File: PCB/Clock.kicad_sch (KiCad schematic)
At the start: 24 parts, among them SW1 SW_Push, SW2 SW_SPDT, U1 LM555xM, U2 LM555xM, U3 LM555xM, U4 74LS08, U5 74LS04, U6 74LS32

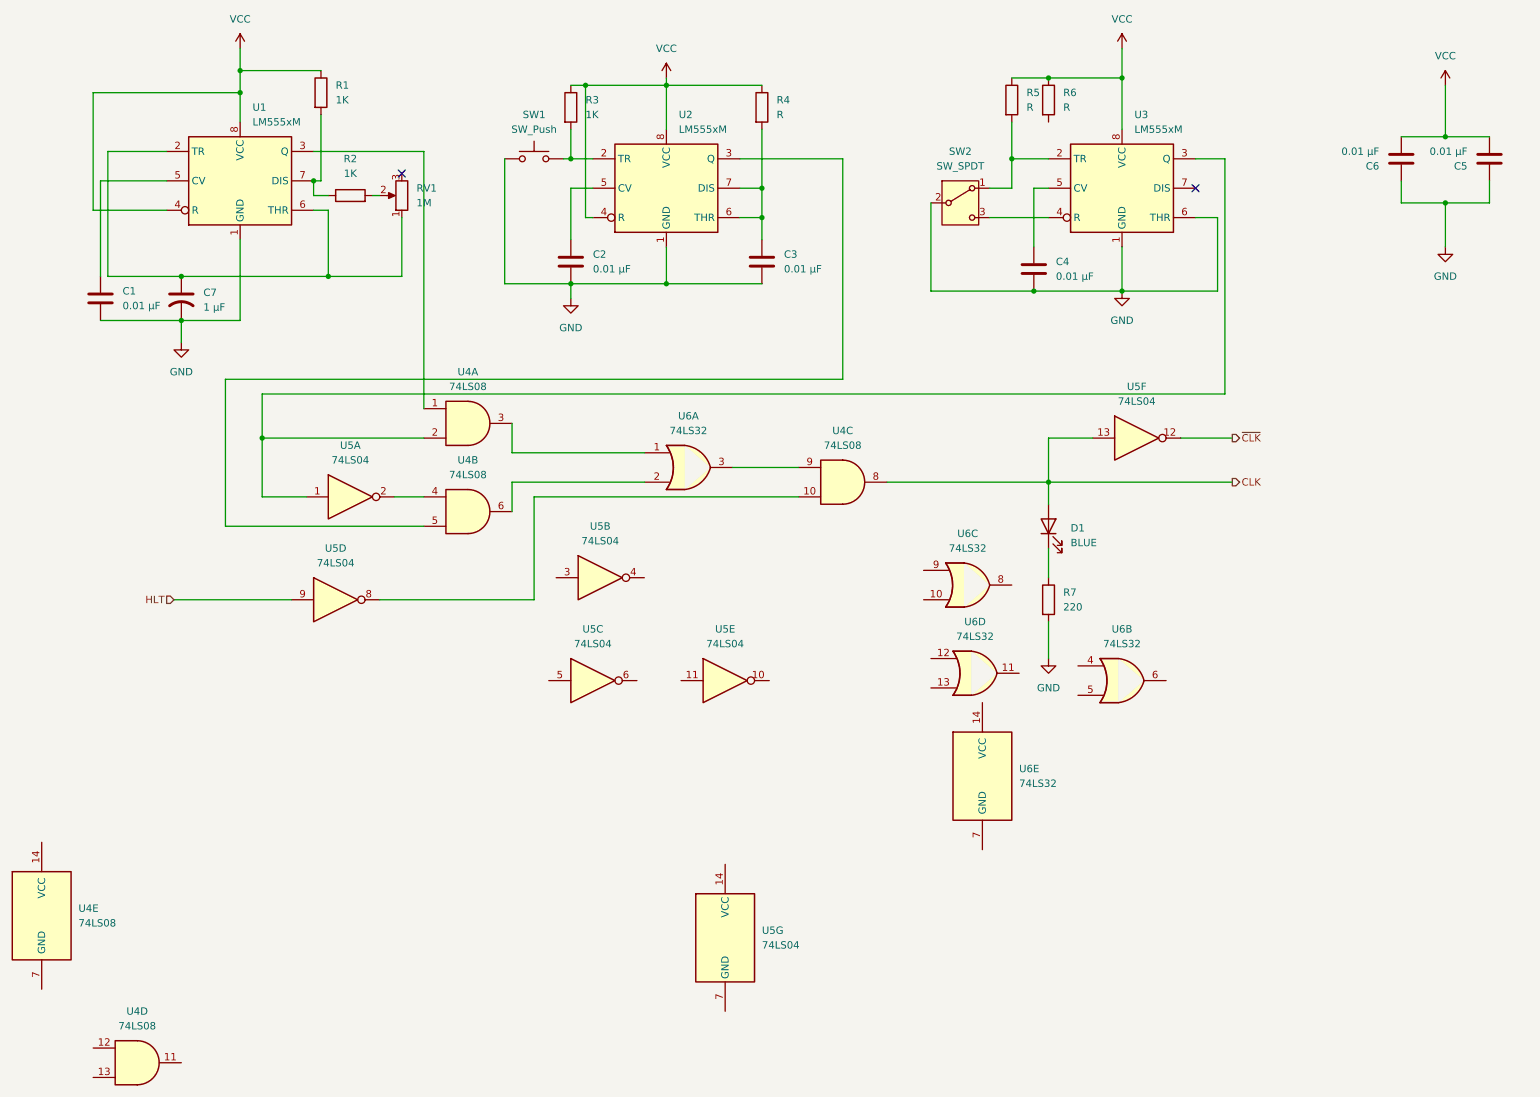
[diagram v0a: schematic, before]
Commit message: Cleaned up the schematic and got started on assigning all the footprints to the symbols
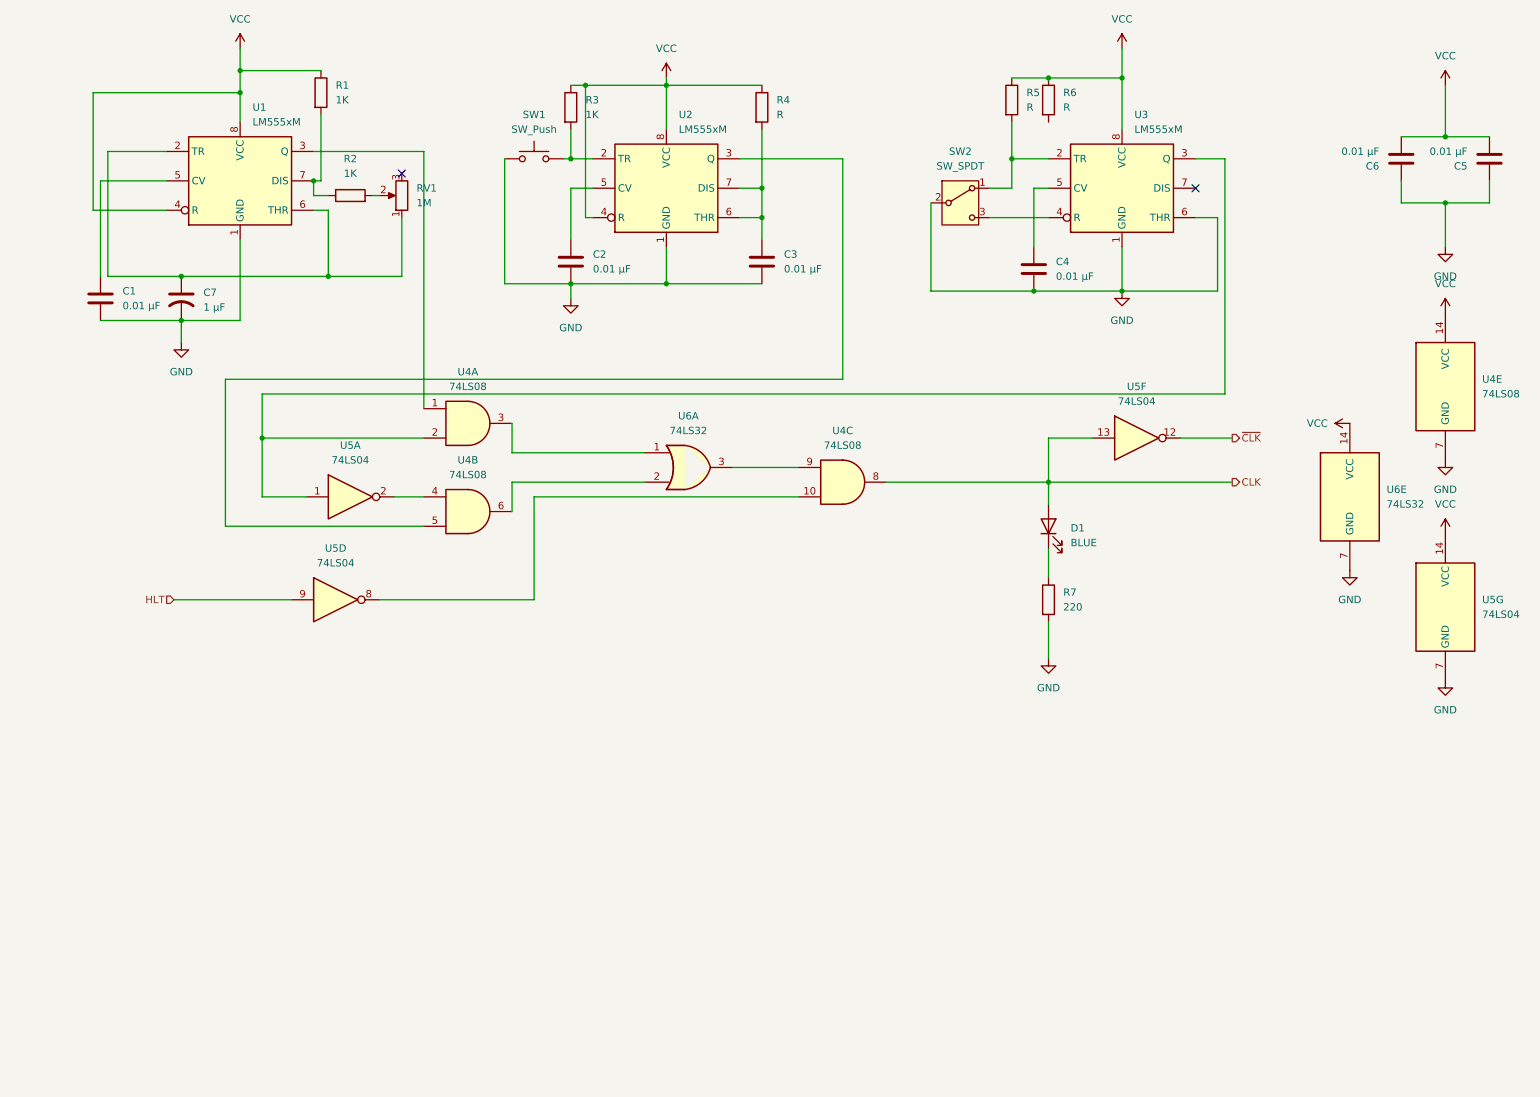
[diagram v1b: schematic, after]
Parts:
- removed unit 4 of U4
- removed unit 3 of U5
- removed unit 2 of U5
- removed unit 5 of U5
- removed unit 2 of U6
- removed unit 3 of U6
- removed unit 4 of U6
- SW1: footprint (none) -> Button_Switch_THT:SW_PUSH_6mm
- SW2: footprint (none) -> Button_Switch_SMD:SW_SPDT_CK_JS102011SAQN
- U6: footprint (none) -> footprints:N14
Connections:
- net GND: now also U4.7 (GND), U5.7 (GND), U6.7 (GND)
- net VCC: now also U4.14 (VCC), U5.14 (VCC), U6.14 (VCC)
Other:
- moved on the sheet: U4E, U5G, U6E

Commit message: added more models to work with on my pcb
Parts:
- R4: value R -> 1M
- R5, R6: value R -> 1K
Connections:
- net at R6.2: now also SW2.3 (C), U3.4 (R)
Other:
- moved on the sheet: C4, R5, R6, SW2
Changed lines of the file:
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@@
-	)
-	(junction
-		(at 193.04 59.69)
-		(diameter 0)
-		(color 0 0 0 0)
 	)
 	(junction
@@
 	)
 	(junction
-		(at 189.23 36.83)
+		(at 264.16 44.45)
 		(diameter 0)
 		(color 0 0 0 0)
 	)
 	(junction
-		(at 264.16 44.45)
+		(at 193.04 22.86)
 		(diameter 0)
 		(color 0 0 0 0)
@@
 	)
 	(junction
-		(at 195.58 22.86)
+		(at 193.04 46.99)
 		(diameter 0)
 		(color 0 0 0 0)
@@
 	)
 	(junction
+		(at 186.69 36.83)
+		(diameter 0)
+		(color 0 0 0 0)
+	)
+	(junction
 		(at 55.88 25.4)
+		(diameter 0)
+		(color 0 0 0 0)
+	)
+	(junction
+		(at 194.31 59.69)
 		(diameter 0)
 		(color 0 0 0 0)
@@
 	(wire
 		(pts
-			(xy 189.23 36.83) (xy 189.23 41.91)
+			(xy 186.69 36.83) (xy 186.69 41.91)
 		)
 		(stroke
@@
 	(wire
 		(pts
-			(xy 185.42 46.99) (xy 195.58 46.99)
+			(xy 182.88 46.99) (xy 193.04 46.99)
 		)
 		(stroke
@@
 	(wire
 		(pts
+			(xy 194.31 41.91) (xy 195.58 41.91)
+		)
+		(stroke
+			(width 0)
+			(type default)
+		)
+	)
+	(wire
+		(pts
 			(xy 45.72 57.15) (xy 71.12 57.15)
 		)
@@
 	(wire
 		(pts
+			(xy 193.04 46.99) (xy 195.58 46.99)
+		)
+		(stroke
+			(width 0)
+			(type default)
+		)
+	)
+	(wire
+		(pts
 			(xy 271.78 44.45) (xy 264.16 44.45)
 		)
@@
 	(wire
 		(pts
-			(xy 195.58 41.91) (xy 193.04 41.91)
-		)
-		(stroke
-			(width 0)
-			(type default)
-		)
-	)
-	(wire
-		(pts
 			(xy 87.63 35.56) (xy 68.58 35.56)
 		)
@@
 	(wire
 		(pts
-			(xy 189.23 30.48) (xy 189.23 36.83)
+			(xy 186.69 30.48) (xy 186.69 36.83)
 		)
 		(stroke
@@
 	(wire
 		(pts
-			(xy 193.04 59.69) (xy 208.28 59.69)
-		)
-		(stroke
-			(width 0)
-			(type default)
-		)
-	)
-	(wire
-		(pts
 			(xy 69.85 29.21) (xy 69.85 40.64)
 		)
@@
 	(wire
 		(pts
+			(xy 193.04 22.86) (xy 208.28 22.86)
+		)
+		(stroke
+			(width 0)
+			(type default)
+		)
+	)
+	(wire
+		(pts
 			(xy 129.54 58.42) (xy 113.03 58.42)
 		)
@@
 	(wire
 		(pts
-			(xy 175.26 44.45) (xy 175.26 59.69)
+			(xy 172.72 44.45) (xy 172.72 59.69)
 		)
 		(stroke
@@
 	(wire
 		(pts
-			(xy 189.23 36.83) (xy 195.58 36.83)
-		)
-		(stroke
-			(width 0)
-			(type default)
-		)
-	)
-	(wire
-		(pts
 			(xy 160.02 36.83) (xy 160.02 74.93)
 		)
@@
 	(wire
 		(pts
+			(xy 193.04 30.48) (xy 193.04 46.99)
+		)
+		(stroke
+			(width 0)
+			(type default)
+		)
+	)
+	(wire
+		(pts
 			(xy 102.87 92.71) (xy 125.73 92.71)
 		)
@@
 	(wire
 		(pts
-			(xy 195.58 22.86) (xy 208.28 22.86)
-		)
-		(stroke
-			(width 0)
-			(type default)
-		)
-	)
-	(wire
-		(pts
 			(xy 53.34 100.33) (xy 87.63 100.33)
 		)
@@
 	(wire
 		(pts
-			(xy 189.23 22.86) (xy 195.58 22.86)
+			(xy 186.69 22.86) (xy 193.04 22.86)
 		)
 		(stroke
@@
 	(wire
 		(pts
-			(xy 189.23 41.91) (xy 185.42 41.91)
+			(xy 186.69 41.91) (xy 182.88 41.91)
 		)
 		(stroke
@@
 	(wire
 		(pts
+			(xy 194.31 59.69) (xy 208.28 59.69)
+		)
+		(stroke
+			(width 0)
+			(type default)
+		)
+	)
+	(wire
+		(pts
 			(xy 55.88 21.59) (xy 55.88 25.4)
 		)
@@
 	(wire
 		(pts
-			(xy 193.04 41.91) (xy 193.04 52.07)
+			(xy 186.69 36.83) (xy 195.58 36.83)
+		)
+		(stroke
+			(width 0)
+			(type default)
+		)
+	)
+	(wire
+		(pts
+			(xy 194.31 41.91) (xy 194.31 52.07)
 		)
 		(stroke
@@
 	(wire
 		(pts
-			(xy 175.26 59.69) (xy 193.04 59.69)
+			(xy 172.72 59.69) (xy 194.31 59.69)
 		)
 		(stroke
@@
 	(symbol
 		(lib_id "Device:C")
-		(at 193.04 55.88 180)
+		(at 194.31 55.88 180)
 		(unit 1)
 		(exclude_from_sim no)
@@
 		(fields_autoplaced yes)
 		(property "Reference" "C4"
-			(at 196.85 54.6099 0)
+			(at 198.12 54.6099 0)
 			(effects
 				(font
@@
 		)
 		(property "Value" "0.01 µF"
-			(at 196.85 57.1499 0)
+			(at 198.12 57.1499 0)
 			(effects
 				(font
@@
 		)
 		(property "Footprint" "Capacitor_THT:C_Disc_D5.0mm_W2.5mm_P2.50mm"
-			(at 192.0748 52.07 0)
+			(at 193.3448 52.07 0)
 			(effects
 				(font
@@
 		)
 		(property "Datasheet" "~"
-			(at 193.04 55.88 0)
+			(at 194.31 55.88 0)
 			(effects
 				(font
@@
 		)
 		(property "Description" "Unpolarized capacitor"
-			(at 193.04 55.88 0)
+			(at 194.31 55.88 0)
 			(effects
 				(font
@@
 	(symbol
 		(lib_id "Device:R")
-		(at 195.58 26.67 0)
+		(at 193.04 26.67 0)
 		(unit 1)
 		(exclude_from_sim no)
@@
 		(fields_autoplaced yes)
 		(property "Reference" "R6"
-			(at 198.12 25.3999 0)
+			(at 195.58 25.3999 0)
 			(effects
 				(font
@@
 			)
 		)
-		(property "Value" "R"
-			(at 198.12 27.9399 0)
+		(property "Value" "1K"
+			(at 195.58 27.9399 0)
 			(effects
 				(font
@@
 		)
 		(property "Footprint" "Resistor_THT:R_Axial_DIN0207_L6.3mm_D2.5mm_P7.62mm_Horizontal"
-			(at 193.802 26.67 90)
+			(at 191.262 26.67 90)
 			(effects
 				(font
@@
 		)
 		(property "Datasheet" "~"
-			(at 195.58 26.67 0)
+			(at 193.04 26.67 0)
 			(effects
 				(font
@@
 		)
 		(property "Description" "Resistor"
-			(at 195.58 26.67 0)
+			(at 193.04 26.67 0)
 			(effects
 				(font
@@
 	(symbol
 		(lib_id "Device:R")
-		(at 189.23 26.67 0)
+		(at 186.69 26.67 0)
 		(unit 1)
 		(exclude_from_sim no)
@@
 		(fields_autoplaced yes)
 		(property "Reference" "R5"
-			(at 191.77 25.3999 0)
+			(at 189.23 25.3999 0)
 			(effects
 				(font
@@
 			)
 		)
-		(property "Value" "R"
-			(at 191.77 27.9399 0)
+		(property "Value" "1K"
+			(at 189.23 27.9399 0)
 			(effects
 				(font
@@
 		)
 		(property "Footprint" "Resistor_THT:R_Axial_DIN0207_L6.3mm_D2.5mm_P7.62mm_Horizontal"
-			(at 187.452 26.67 90)
+			(at 184.912 26.67 90)
 			(effects
 				(font
@@
 		)
 		(property "Datasheet" "~"
-			(at 189.23 26.67 0)
+			(at 186.69 26.67 0)
 			(effects
 				(font
@@
 		)
 		(property "Description" "Resistor"
-			(at 189.23 26.67 0)
+			(at 186.69 26.67 0)
 			(effects
 				(font
@@
 	(symbol
 		(lib_id "Switch:SW_SPDT")
-		(at 180.34 44.45 0)
+		(at 177.8 44.45 0)
 		(unit 1)
 		(exclude_from_sim no)
@@
 		(fields_autoplaced yes)
 		(property "Reference" "SW2"
-			(at 180.34 35.56 0)
+			(at 177.8 35.56 0)
 			(effects
 				(font
@@
 		)
 		(property "Value" "SW_SPDT"
-			(at 180.34 38.1 0)
+			(at 177.8 38.1 0)
 			(effects
 				(font
@@
 		)
 		(property "Footprint" "Button_Switch_SMD:SW_SPDT_CK_JS102011SAQN"
-			(at 180.34 44.45 0)
+			(at 177.8 44.45 0)
 			(effects
 				(font
@@
 		)
 		(property "Datasheet" "~"
-			(at 180.34 52.07 0)
+			(at 177.8 52.07 0)
 			(effects
 				(font
@@
 		)
 		(property "Description" "Switch, single pole double throw"
-			(at 180.34 44.45 0)
+			(at 177.8 44.45 0)
 			(effects
 				(font
@@
 			)
 		)
-		(property "Value" "R"
+		(property "Value" "1M"
 			(at 148.59 29.2099 0)
 			(effects

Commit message: Fixed a bunch of ERC errors so know there is only one remaining.
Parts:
- U6: footprint footprints:N14 -> Package_DIP:DIP-14_W7.62mm
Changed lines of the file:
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@@
 			)
 		)
-		(property "Footprint" "footprints:N14"
+		(property "Footprint" "Package_DIP:DIP-14_W7.62mm"
 			(at 133.35 90.17 0)
 			(effects
@@
 			)
 		)
-		(property "Footprint" "footprints:N14"
+		(property "Footprint" "Package_DIP:DIP-14_W7.62mm"
 			(at 247.65 95.25 0)
 			(effects

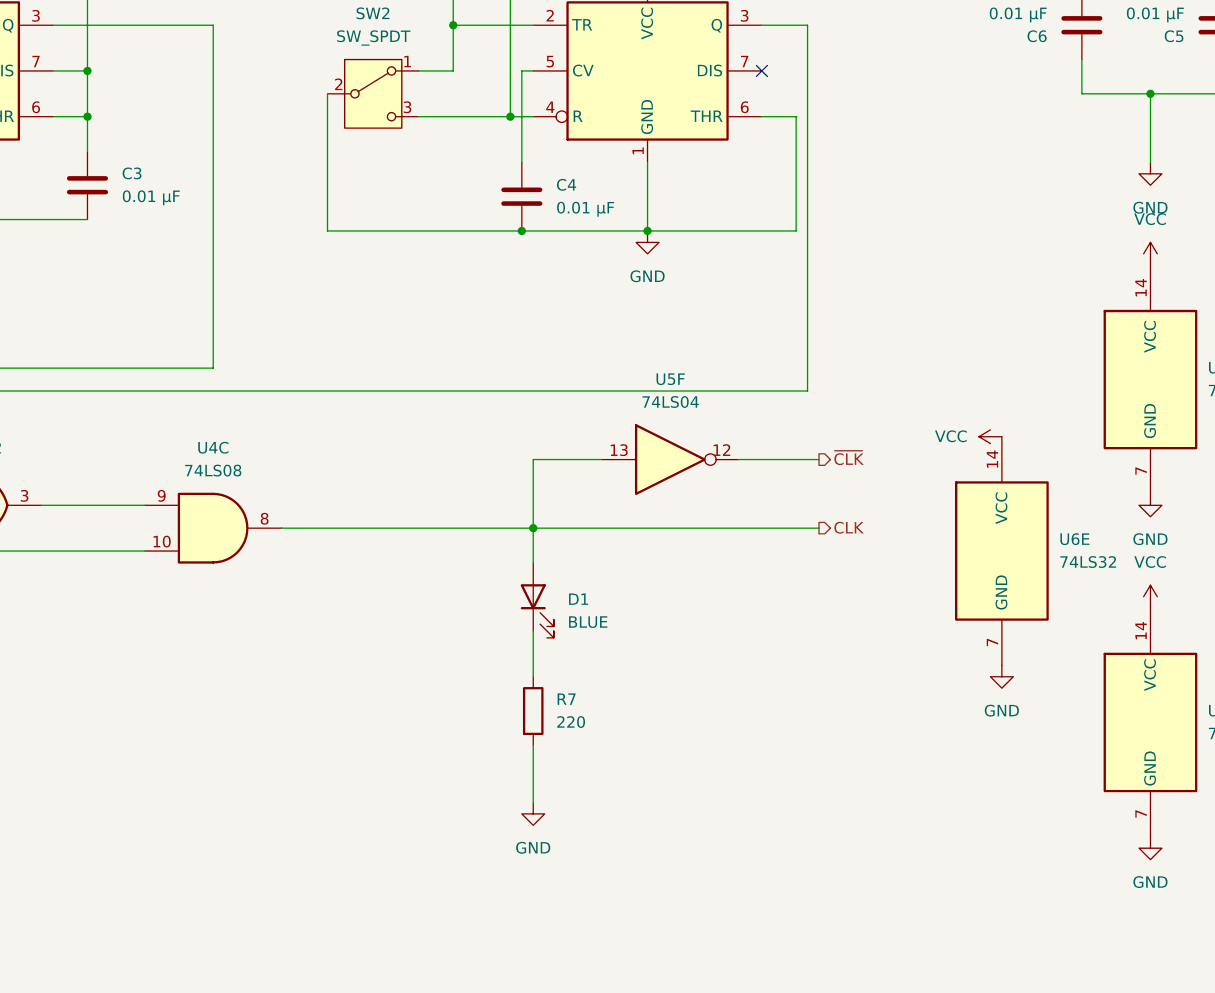
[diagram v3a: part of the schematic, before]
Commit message: Routed the traces for the ground
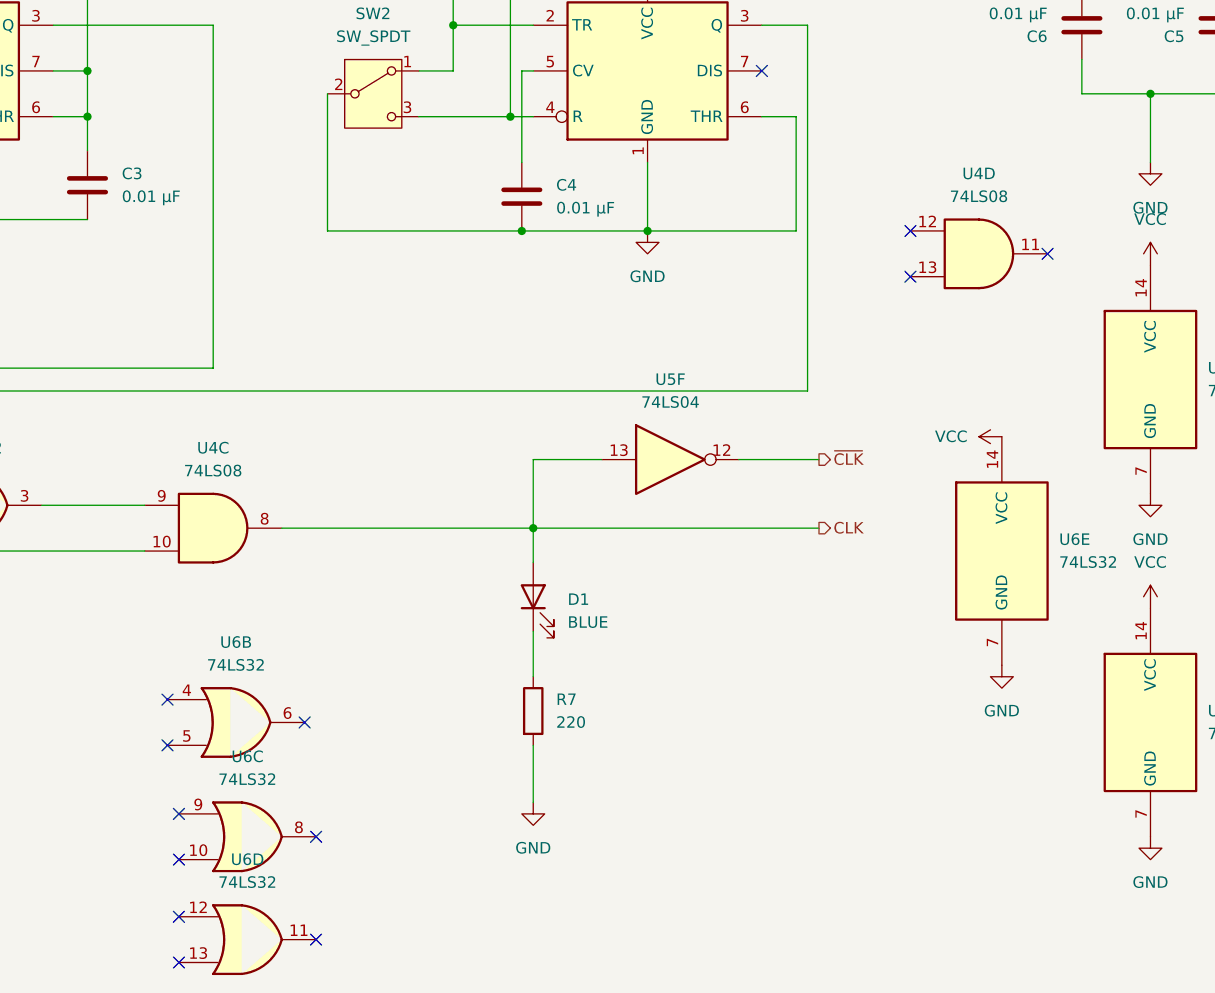
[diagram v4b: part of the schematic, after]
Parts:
- added unit 5 of U4
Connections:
- net GND: now also U4.7 (GND); no longer U4.7 (GND)
- net VCC: now also U4.14 (VCC); no longer U4.14 (VCC)
- no-connect marks 2 -> 14

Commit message: add git ignore
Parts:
- added unit 2 of U6
- added unit 3 of U6
- added unit 4 of U6
